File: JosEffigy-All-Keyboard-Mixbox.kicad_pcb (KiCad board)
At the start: 2 copper layers, 173 x 117.5 mm, 33 parts, among them U1 RP2040

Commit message: Release 1.0
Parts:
- added REF**: MountingHole_2.7mm_M2.5_ISO7380_Pad_TopBottom, MountingHole:MountingHole_2.7mm_M2.5_ISO7380_Pad_TopBottom, F.Cu at (61.0, 156.2)
- added REF**: MountingHole_2.7mm_M2.5_ISO7380_Pad_TopBottom, MountingHole:MountingHole_2.7mm_M2.5_ISO7380_Pad_TopBottom, F.Cu at (229.9, 40.6)
- added REF**: MountingHole_2.7mm_M2.5_ISO7380_Pad_TopBottom, MountingHole:MountingHole_2.7mm_M2.5_ISO7380_Pad_TopBottom, F.Cu at (229.9, 156.2)
- added REF**: MountingHole_2.7mm_M2.5_ISO7380_Pad_TopBottom, MountingHole:MountingHole_2.7mm_M2.5_ISO7380_Pad_TopBottom, F.Cu at (61.0, 40.6)
- D1, D10, D11, D12, D13, D14, D15, D16, D2, D3, D4, D5, D6, D7, D8, D9: footprint LED_SMD:LED_SK6812MINI_PLCC4_3.5x3.5mm_P1.75mm -> kicad-footprints:YS-SK6812MINI-E; moved to B.Cu
- MX1, MX10, MX11, MX12, MX13, MX14, MX15, MX16, MX2, MX3, MX4, MX5, MX6, MX7, MX9: footprint Button_Switch_Keyboard:SW_Cherry_MX_1.00u_Plate -> PCM_Switch_Keyboard_Hotswap_Kailh:SW_Hotswap_Kailh_MX_Plated_1.00u
- MX8: footprint Button_Switch_Keyboard:SW_Cherry_MX_2.00u_Plate -> PCM_Switch_Keyboard_Hotswap_Kailh:SW_Hotswap_Kailh_MX_Plated_2.00u
- moved D8 14.1 mm to (137.3, 152.2)
- moved D10 13.8 mm to (184.2, 113.8), turned to 180 degrees
- moved D11 13.8 mm to (203.2, 113.8), turned to 0 degrees
- moved D14 13.5 mm to (184.2, 94.5), turned to 180 degrees
- moved D15 13.5 mm to (203.2, 94.5), turned to 180 degrees
- moved D13 13.5 mm to (165.1, 100.0), turned to 0 degrees
- moved D16 13.5 mm to (222.2, 100.0), turned to 180 degrees
- moved D12 13.5 mm to (222.2, 119.1), turned to 180 degrees
- moved D9 13.5 mm to (165.3, 119.1), turned to 0 degrees
- moved D5 13.4 mm to (70.6, 66.5), turned to 180 degrees
- moved D6 13.4 mm to (90.3, 66.5), turned to 180 degrees
- moved D7 13.4 mm to (108.7, 66.5), turned to 180 degrees
- moved D3 12.3 mm to (108.0, 115.4)
- moved D1 12.2 mm to (70.5, 107.3), turned to 168 degrees
- moved D2 12.2 mm to (89.4, 111.3), turned to 168 degrees
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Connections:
- MX10 pad 1: unconnected-(MX10-COL-Pad1) -> GND
- MX11 pad 1: unconnected-(MX11-COL-Pad1) -> GND
- MX13 pad 1: unconnected-(MX13-COL-Pad1) -> GND
- MX14 pad 1: unconnected-(MX14-COL-Pad1) -> GND
- MX15 pad 1: unconnected-(MX15-COL-Pad1) -> GND
- MX16 pad 1: unconnected-(MX16-COL-Pad1) -> GND
- MX4 pad 2: unconnected-(MX4-ROW-Pad2) -> UP
- MX6 pad 1: unconnected-(MX6-COL-Pad1) -> GND
- MX9 pad 1: unconnected-(MX9-COL-Pad1) -> GND
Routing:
- net GND: track 530.0 -> 606.9 mm, vias 1 -> 0
- net Net-(D12-DOUT): track 109.0 -> 66.9 mm, vias 0 -> 2
- net UP: track 144.7 -> 186.7 mm, vias 0 -> 1
- net VCC: track 393.5 -> 421.9 mm, vias 2 -> 3
- net 1K: track 84.5 -> 67.6 mm, vias 0 -> 1
- net 2K: track 62.6 -> 47.2 mm, vias 0 -> 1
- net 4K: track 54.7 -> 68.4 mm
- net Net-(D7-DOUT): track 99.5 -> 112.5 mm, vias 2 -> 0
- net 4P: track 56.7 -> 45.8 mm
- net HOME: track 137.0 -> 127.4 mm
- net 2P: track 29.1 -> 20.5 mm
- net Net-(D1-DOUT): track 36.6 -> 28.3 mm
- net 1P: track 50.9 -> 42.9 mm
- net Net-(D3-DOUT): track 39.7 -> 31.8 mm
- net RIGHT: track 132.0 -> 124.3 mm, vias 1 -> 0
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- added copper zone on B.Cu, net GND
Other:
- board size 173 x 117.5 mm -> 176.5 x 123.2 mm

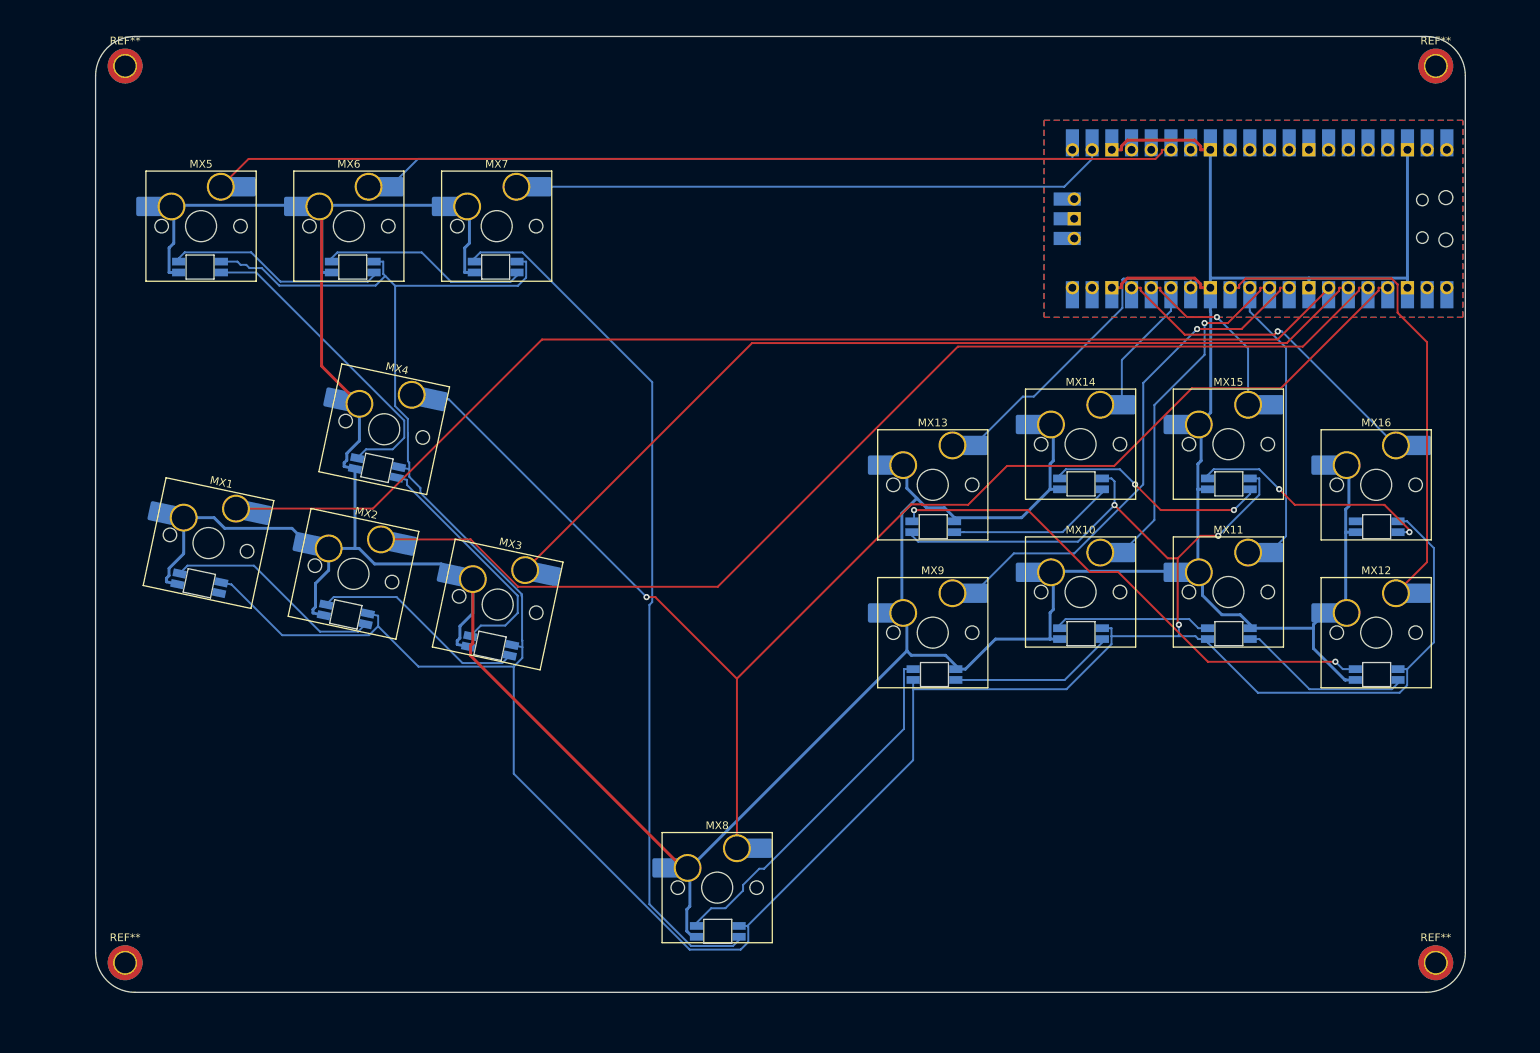
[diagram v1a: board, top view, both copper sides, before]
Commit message: Release 1.0b
Moved power to VBUS, added DTranslator, added Capacitors
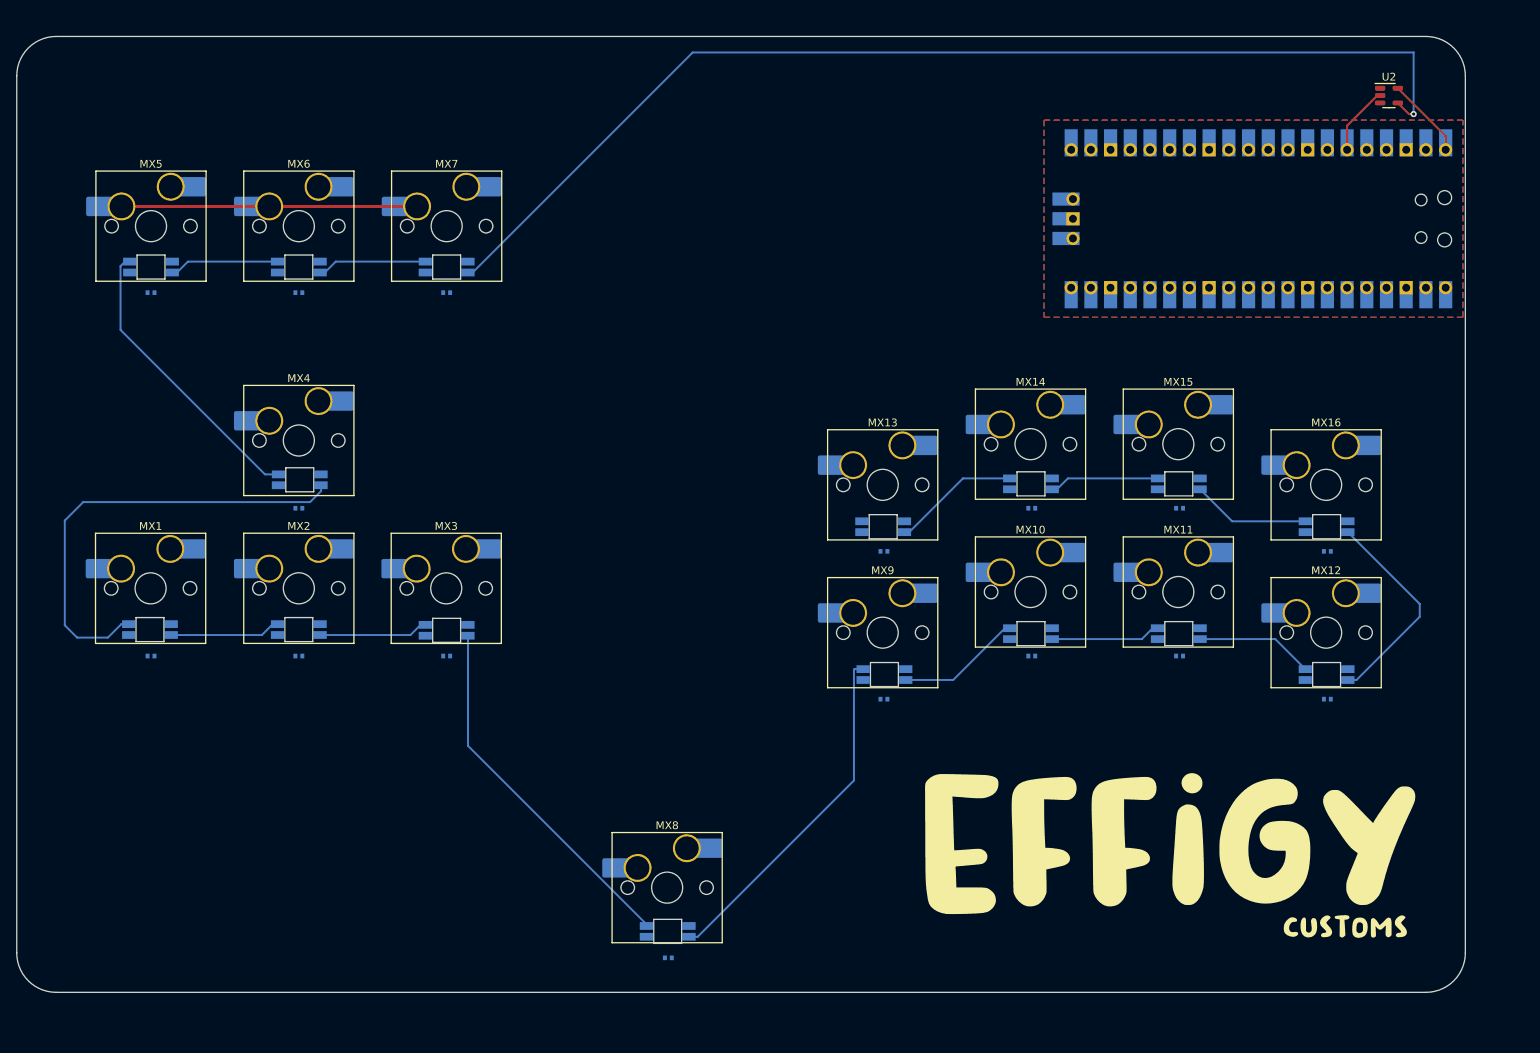
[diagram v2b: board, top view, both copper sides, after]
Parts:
- removed REF** (x4): MountingHole_2.7mm_M2.5_ISO7380_Pad_TopBottom, MountingHole:MountingHole_2.7mm_M2.5_ISO7380_Pad_TopBottom
- added C1: 100nf, CAPC1005X55N:CAPC1005X55N, B.Cu at (102.4, 69.8)
- added C10: 100nf, CAPC1005X55N:CAPC1005X55N, B.Cu at (177.8, 116.7)
- added C11: 100nf, CAPC1005X55N:CAPC1005X55N, B.Cu at (196.8, 116.7)
- added C12: 100nf, CAPC1005X55N:CAPC1005X55N, B.Cu at (215.9, 122.2)
- added C13: 100nf, CAPC1005X55N:CAPC1005X55N, B.Cu at (158.8, 103.2)
- added C14: 100nf, CAPC1005X55N:CAPC1005X55N, B.Cu at (177.8, 97.6)
- added C15: 100nf, CAPC1005X55N:CAPC1005X55N, B.Cu at (196.8, 97.6)
- added C16: 100nf, CAPC1005X55N:CAPC1005X55N, B.Cu at (215.9, 103.2)
- added C2: 100nf, CAPC1005X55N:CAPC1005X55N, B.Cu at (83.3, 69.8)
- added C3: 100nf, CAPC1005X55N:CAPC1005X55N, B.Cu at (64.3, 69.8)
- added C4: 100nf, CAPC1005X55N:CAPC1005X55N, B.Cu at (64.3, 116.7)
- added C5: 100nf, CAPC1005X55N:CAPC1005X55N, B.Cu at (83.3, 116.7)
- added C6: 100nf, CAPC1005X55N:CAPC1005X55N, B.Cu at (102.4, 116.7)
- added C7: 100nf, CAPC1005X55N:CAPC1005X55N, B.Cu at (131.0, 155.6)
- added C8: 100nf, CAPC1005X55N:CAPC1005X55N, B.Cu at (83.3, 97.6)
- added C9: 100nf, CAPC1005X55N:CAPC1005X55N, B.Cu at (158.8, 122.2)
- added G***: LOGO, LOGO, F.Cu at (195.6, 141.0)
- added U2: SN74LV1T34DBV, Package_TO_SOT_SMD:SOT-23-5, F.Cu at (223.8, 44.5)
- U1: value RP2040 -> Pico
- moved MX4 11.1 mm to (83.3, 88.9), turned to 0 degrees
- moved D4 10.1 mm to (83.5, 94.0), turned to 0 degrees
- moved MX1 9.47 mm to (64.2, 108.0), turned to 0 degrees
- moved D1 8.72 mm to (64.2, 113.3), turned to 0 degrees
- moved MX2 7.29 mm to (83.3, 108.0), turned to 0 degrees
- moved D6 6.95 mm to (83.3, 66.5)
- moved MX3 6.95 mm to (102.3, 108.0), turned to 0 degrees
- moved MX12 6.45 mm to (215.7, 113.7)
- moved MX13 6.45 mm to (158.6, 94.6)
- moved MX16 6.45 mm to (215.7, 94.6)
- moved MX9 6.45 mm to (158.6, 113.7)
- moved MX6 6.45 mm to (83.3, 61.3)
- moved MX7 6.45 mm to (102.4, 61.3)
- moved D10 6.45 mm to (177.7, 113.8), turned to 0 degrees
- moved D11 6.45 mm to (196.7, 113.8)
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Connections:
- D1 pad 3: RGB0 -> Net-(D1-DIN)
- D13 pad 1: Net-(D13-DOUT) -> unconnected-(D13-DOUT-Pad1)
- D13 pad 3: Net-(D12-DOUT) -> Net-(D13-DIN)
- D14 pad 1: Net-(D14-DOUT) -> Net-(D13-DIN)
- D14 pad 3: Net-(D13-DOUT) -> Net-(D14-DIN)
- D15 pad 1: Net-(D15-DOUT) -> Net-(D14-DIN)
- D15 pad 3: Net-(D14-DOUT) -> Net-(D15-DIN)
- D16 pad 1: unconnected-(D16-DOUT-Pad1) -> Net-(D15-DIN)
- D16 pad 3: Net-(D15-DOUT) -> Net-(D12-DOUT)
- U1 pad 35: unconnected-(U1-GPIO23-Pad35) -> RGB0
- U1 pad 40: unconnected-(U1-GPIO28_ADC2-Pad40) -> VCC
- U1 pad 8: GND -> unconnected-(U1-GND-Pad8)
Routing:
- net GND: track 606.9 -> 38.1 mm
- net VCC: track 421.9 -> 10.5 mm, vias 3 -> 0
- net Net-(D1-DIN): track 0.00 -> 202.6 mm, vias 0 -> 1
- net UP: track 186.7 -> 0.00 mm, vias 1 -> 0
- net LEFT: track 155.6 -> 0.00 mm
- net DOWN: track 148.9 -> 0.00 mm
- net HOME: track 127.4 -> 0.00 mm
- net RIGHT: track 124.3 -> 0.00 mm
- net Net-(D7-DOUT): track 112.5 -> 0.00 mm
- net SELECT: track 93.4 -> 0.00 mm
- net START: track 76.9 -> 0.00 mm
- net 4K: track 68.4 -> 0.00 mm
- net 1K: track 67.6 -> 0.00 mm, vias 1 -> 0
- net Net-(D3-DOUT): track 31.8 -> 84.6 mm
- net 2K: track 47.2 -> 0.00 mm, vias 1 -> 0
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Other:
- board size 176.5 x 123.2 mm -> 186.7 x 123.2 mm

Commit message: Release 1.0c
redid the routing
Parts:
- U2: moved to B.Cu
- moved U2 4.76 mm to (219.1, 44.5), turned to 180 degrees
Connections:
- D4 pad 1: Net-(D4-DOUT) -> Net-(D1-DIN)
- D4 pad 3: Net-(D3-DOUT) -> Net-(D4-DIN)
- D5 pad 1: Net-(D5-DOUT) -> Net-(D4-DIN)
- D5 pad 3: Net-(D4-DOUT) -> Net-(D5-DIN)
- D6 pad 1: Net-(D6-DOUT) -> Net-(D5-DIN)
- D6 pad 3: Net-(D5-DOUT) -> Net-(D6-DIN)
- D7 pad 1: Net-(D7-DOUT) -> Net-(D6-DIN)
- D7 pad 3: Net-(D6-DOUT) -> Net-(D7-DIN)
- D8 pad 3: Net-(D7-DOUT) -> Net-(D3-DOUT)
- U2 pad 4: Net-(D1-DIN) -> Net-(D7-DIN)
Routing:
- net VCC: track 10.5 -> 634.9 mm, vias 0 -> 2
- net GND: track 38.1 -> 524.0 mm, vias 0 -> 34
- net UP: track 0.00 -> 225.8 mm, vias 0 -> 1
- net Net-(D1-DIN): track 202.6 -> 34.1 mm, vias 1 -> 0
- net LEFT: track 0.00 -> 167.6 mm
- net DOWN: track 0.00 -> 153.8 mm
- net HOME: track 0.00 -> 134.7 mm
- net RIGHT: track 0.00 -> 130.9 mm
- net Net-(D7-DIN): track 0.00 -> 130.4 mm, vias 0 -> 2
- net SELECT: track 0.00 -> 101.7 mm
- net START: track 0.00 -> 85.5 mm
- net 1K: track 0.00 -> 81.2 mm
- net 2K: track 0.00 -> 58.7 mm, vias 0 -> 1
- net 4K: track 0.00 -> 49.6 mm, vias 0 -> 1
- net 1P: track 0.00 -> 48.4 mm
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
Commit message: Release 1.0d
I think It's ready
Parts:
- added REF**: MountingHole_2.1mm, MountingHole:MountingHole_2.1mm, F.Cu at (50.8, 156.4)
- added REF**: MountingHole_2.1mm, MountingHole:MountingHole_2.1mm, F.Cu at (230.2, 40.5)
- added REF**: MountingHole_2.1mm, MountingHole:MountingHole_2.1mm, F.Cu at (230.2, 156.4)
- added REF**: MountingHole_2.1mm, MountingHole:MountingHole_2.1mm, F.Cu at (50.8, 40.5)
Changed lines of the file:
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@@
     )
+  )
+  (footprint "MountingHole:MountingHole_2.1mm" (layer "F.Cu")
+    (at 50.8 156.36875)
+    (descr "Mounting Hole 2.1mm, no annular")
+    (tags "mounting hole 2.1mm no annular")
+    (attr exclude_from_pos_files exclude_from_bom)
+    (fp_text reference "REF**" (at 0 -3.2) (layer "F.SilkS") hide
+        (effects (font (size 1 1) (thickness 0.15)))
+    )
+    (fp_text value "MountingHole_2.1mm" (at 0 3.2) (layer "F.Fab")
+        (effects (font (size 1 1) (thickness 0.15)))
+    )
+    (fp_text user "${REFERENCE}" (at 0 0) (layer "F.Fab")
+        (effects (font (size 1 1) (thickness 0.15)))
+    )
+    (fp_circle (center 0 0) (end 2.1 0)
+      (stroke (width 0.15) (type solid)) (fill none) (layer "Cmts.User"))
+    (fp_circle (center 0 0) (end 2.35 0)
+      (stroke (width 0.05) (type solid)) (fill none) (layer "F.CrtYd"))
+    (pad "" np_thru_hole circle (at 0 0) (size 2.1 2.1) (drill 2.1) (layers "*.Cu" "*.Mask"))
   )
   (footprint "PCM_Switch_Keyboard_Hotswap_Kailh:SW_Hotswap_Kailh_MX_Plated_1.00u" (layer "F.Cu")
@@
     )
   )
+  (footprint "MountingHole:MountingHole_2.1mm" (layer "F.Cu")
+    (at 230.1875 40.48125)
+    (descr "Mounting Hole 2.1mm, no annular")
+    (tags "mounting hole 2.1mm no annular")
+    (attr exclude_from_pos_files exclude_from_bom)
+    (fp_text reference "REF**" (at 0 -3.2) (layer "F.SilkS") hide
+        (effects (font (size 1 1) (thickness 0.15)))
+    )
+    (fp_text value "MountingHole_2.1mm" (at 0 3.2) (layer "F.Fab")
+        (effects (font (size 1 1) (thickness 0.15)))
+    )
+    (fp_text user "${REFERENCE}" (at 0 0) (layer "F.Fab")
+        (effects (font (size 1 1) (thickness 0.15)))
+    )
+    (fp_circle (center 0 0) (end 2.1 0)
+      (stroke (width 0.15) (type solid)) (fill none) (layer "Cmts.User"))
+    (fp_circle (center 0 0) (end 2.35 0)
+      (stroke (width 0.05) (type solid)) (fill none) (layer "F.CrtYd"))
+    (pad "" np_thru_hole circle (at 0 0) (size 2.1 2.1) (drill 2.1) (layers "*.Cu" "*.Mask"))
+  )
   (footprint "PCM_Switch_Keyboard_Hotswap_Kailh:SW_Hotswap_Kailh_MX_Plated_1.00u" (layer "F.Cu")
     (at 158.5912 94.615)
@@
     )
   )
+  (footprint "MountingHole:MountingHole_2.1mm" (layer "F.Cu")
+    (at 230.1875 156.36875)
+    (descr "Mounting Hole 2.1mm, no annular")
+    (tags "mounting hole 2.1mm no annular")
+    (attr exclude_from_pos_files exclude_from_bom)
+    (fp_text reference "REF**" (at 0 -3.2) (layer "F.SilkS") hide
+        (effects (font (size 1 1) (thickness 0.15)))
+    )
+    (fp_text value "MountingHole_2.1mm" (at 0 3.2) (layer "F.Fab")
+        (effects (font (size 1 1) (thickness 0.15)))
+    )
+    (fp_text user "${REFERENCE}" (at 0 0) (layer "F.Fab")
+        (effects (font (size 1 1) (thickness 0.15)))
+    )
+    (fp_circle (center 0 0) (end 2.1 0)
+      (stroke (width 0.15) (type solid)) (fill none) (layer "Cmts.User"))
+    (fp_circle (center 0 0) (end 2.35 0)
+      (stroke (width 0.05) (type solid)) (fill none) (layer "F.CrtYd"))
+    (pad "" np_thru_hole circle (at 0 0) (size 2.1 2.1) (drill 2.1) (layers "*.Cu" "*.Mask"))
+  )
+  (footprint "MountingHole:MountingHole_2.1mm" (layer "F.Cu")
+    (at 50.8 40.48125)
+    (descr "Mounting Hole 2.1mm, no annular")
+    (tags "mounting hole 2.1mm no annular")
+    (attr exclude_from_pos_files exclude_from_bom)
+    (fp_text reference "REF**" (at 0 -3.2) (layer "F.SilkS") hide
+        (effects (font (size 1 1) (thickness 0.15)))
+    )
+    (fp_text value "MountingHole_2.1mm" (at 0 3.2) (layer "F.Fab")
+        (effects (font (size 1 1) (thickness 0.15)))
+    )
+    (fp_text user "${REFERENCE}" (at 0 0) (layer "F.Fab")
+        (effects (font (size 1 1) (thickness 0.15)))
+    )
+    (fp_circle (center 0 0) (end 2.1 0)
+      (stroke (width 0.15) (type solid)) (fill none) (layer "Cmts.User"))
+    (fp_circle (center 0 0) (end 2.35 0)
+      (stroke (width 0.05) (type solid)) (fill none) (layer "F.CrtYd"))
+    (pad "" np_thru_hole circle (at 0 0) (size 2.1 2.1) (drill 2.1) (layers "*.Cu" "*.Mask"))
+  )
   (footprint "PCM_Switch_Keyboard_Hotswap_Kailh:SW_Hotswap_Kailh_MX_Plated_1.00u" (layer "F.Cu")

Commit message: Release 1.0d
re-commit, added
production folder
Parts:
- removed the REF** at (50.8, 156.4)
- removed the REF** at (230.2, 40.5)
- removed the REF** at (230.2, 156.4)
- removed the REF** at (50.8, 40.5)
- added REF**: MountingHole_2.2mm_M2, MountingHole:MountingHole_2.2mm_M2, F.Cu at (50.8, 156.2)
- added REF**: MountingHole_2.2mm_M2, MountingHole:MountingHole_2.2mm_M2, F.Cu at (50.8, 40.6)
- added REF**: MountingHole_2.2mm_M2, MountingHole:MountingHole_2.2mm_M2, F.Cu at (229.9, 40.6)
- added REF**: MountingHole_2.2mm_M2, MountingHole:MountingHole_2.2mm_M2, F.Cu at (229.9, 156.2)
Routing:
- net GND: track 524.0 -> 0.00 mm, vias 34 -> 0
- net VCC: track 634.9 -> 571.4 mm, vias 2 -> 0
- net Net-(D4-DIN): track 41.6 -> 86.9 mm
- net 3K: track 46.5 -> 38.5 mm, vias 1 -> 0
- net Net-(D13-DIN): track 22.3 -> 16.4 mm, vias 2 -> 0
- net Net-(D12-DOUT): track 24.9 -> 30.6 mm, vias 2 -> 0
- net Net-(D7-DIN): track 130.4 -> 124.9 mm
- net Net-(D14-DIN): track 18.9 -> 14.1 mm, vias 2 -> 0
- net 4P: track 45.2 -> 41.2 mm, vias 2 -> 1
- net 2K: track 58.7 -> 62.3 mm, vias 1 -> 0
- net Net-(D5-DIN): track 17.5 -> 14.1 mm, vias 2 -> 0
- net 4K: track 49.6 -> 52.8 mm, vias 1 -> 0
- net UP: track 225.8 -> 223.4 mm
- net START: track 85.5 -> 83.1 mm
- net SELECT: track 101.7 -> 99.7 mm
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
